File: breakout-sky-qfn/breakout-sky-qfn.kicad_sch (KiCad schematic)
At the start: 77 parts, among them J1 DF40C-50DS-0.4V_51, J2 DF40C-20DS-0.4V_51, J3 Conn_01x12, J4 Conn_01x12, J5 DF40C-40DS-0.4V_51, J7 DF40C-20DS-0.4V_51, U1 Openframe_QFN_TT06_REV2, U2 24LC02, U3 AP2112K-1.8, U4 AP2112K-1.8

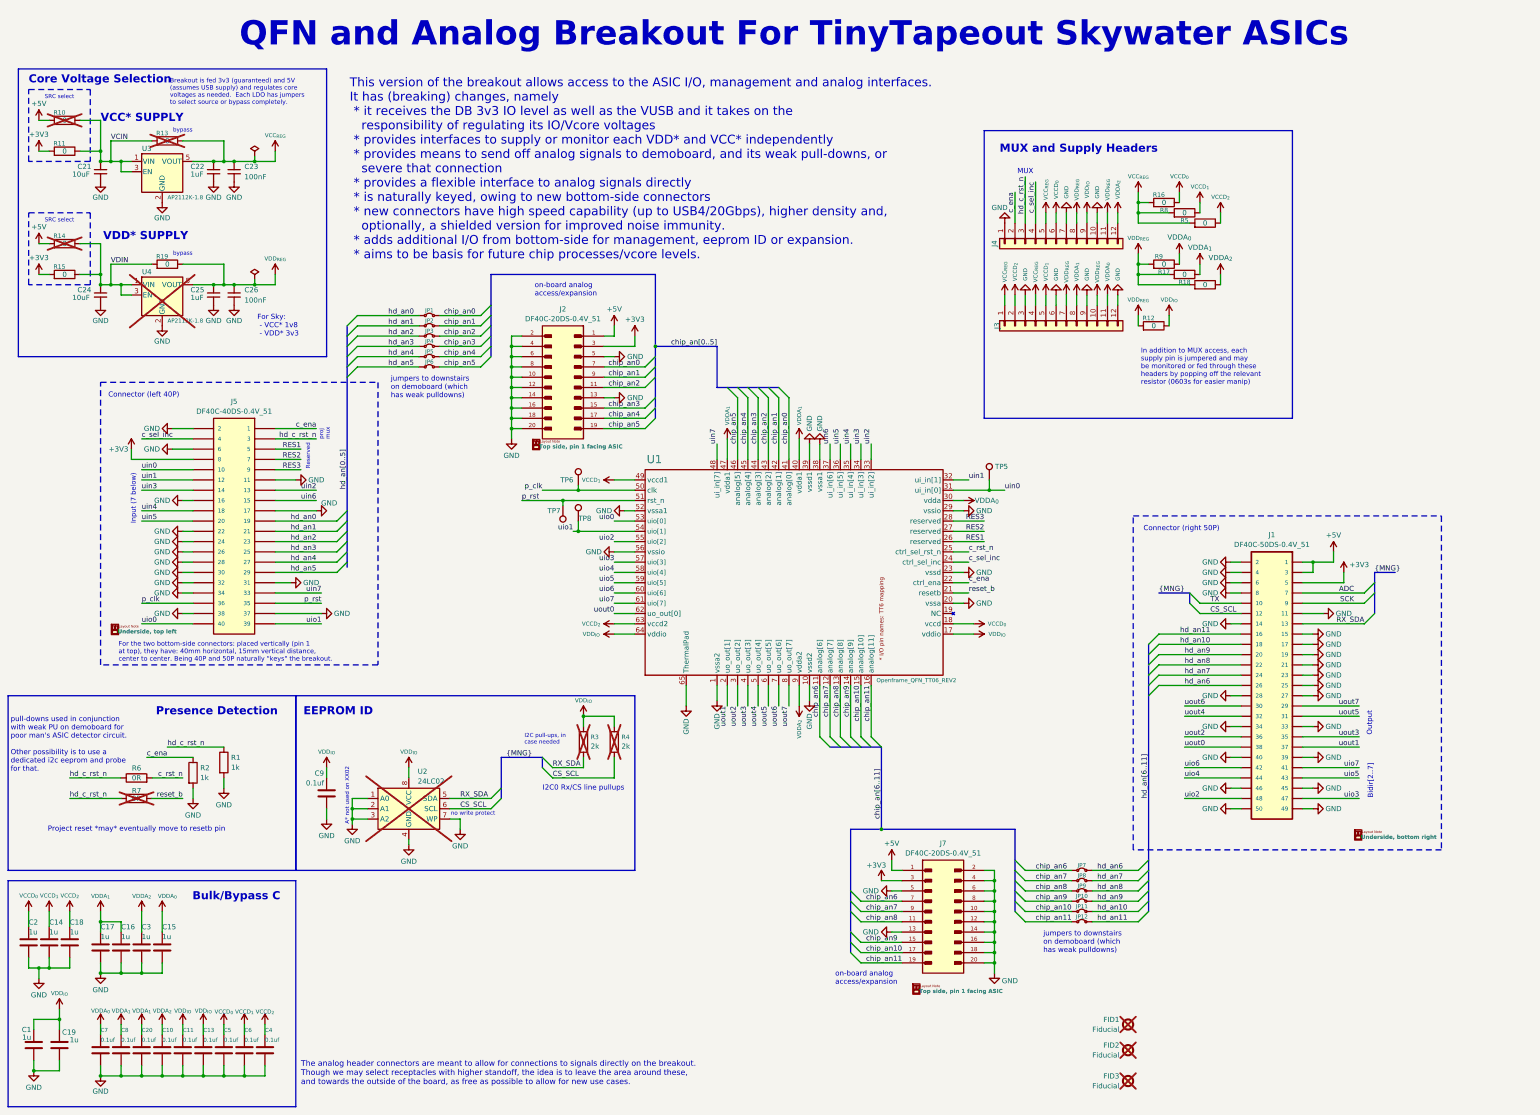
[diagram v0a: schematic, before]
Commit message: increased size of power rail jumpers
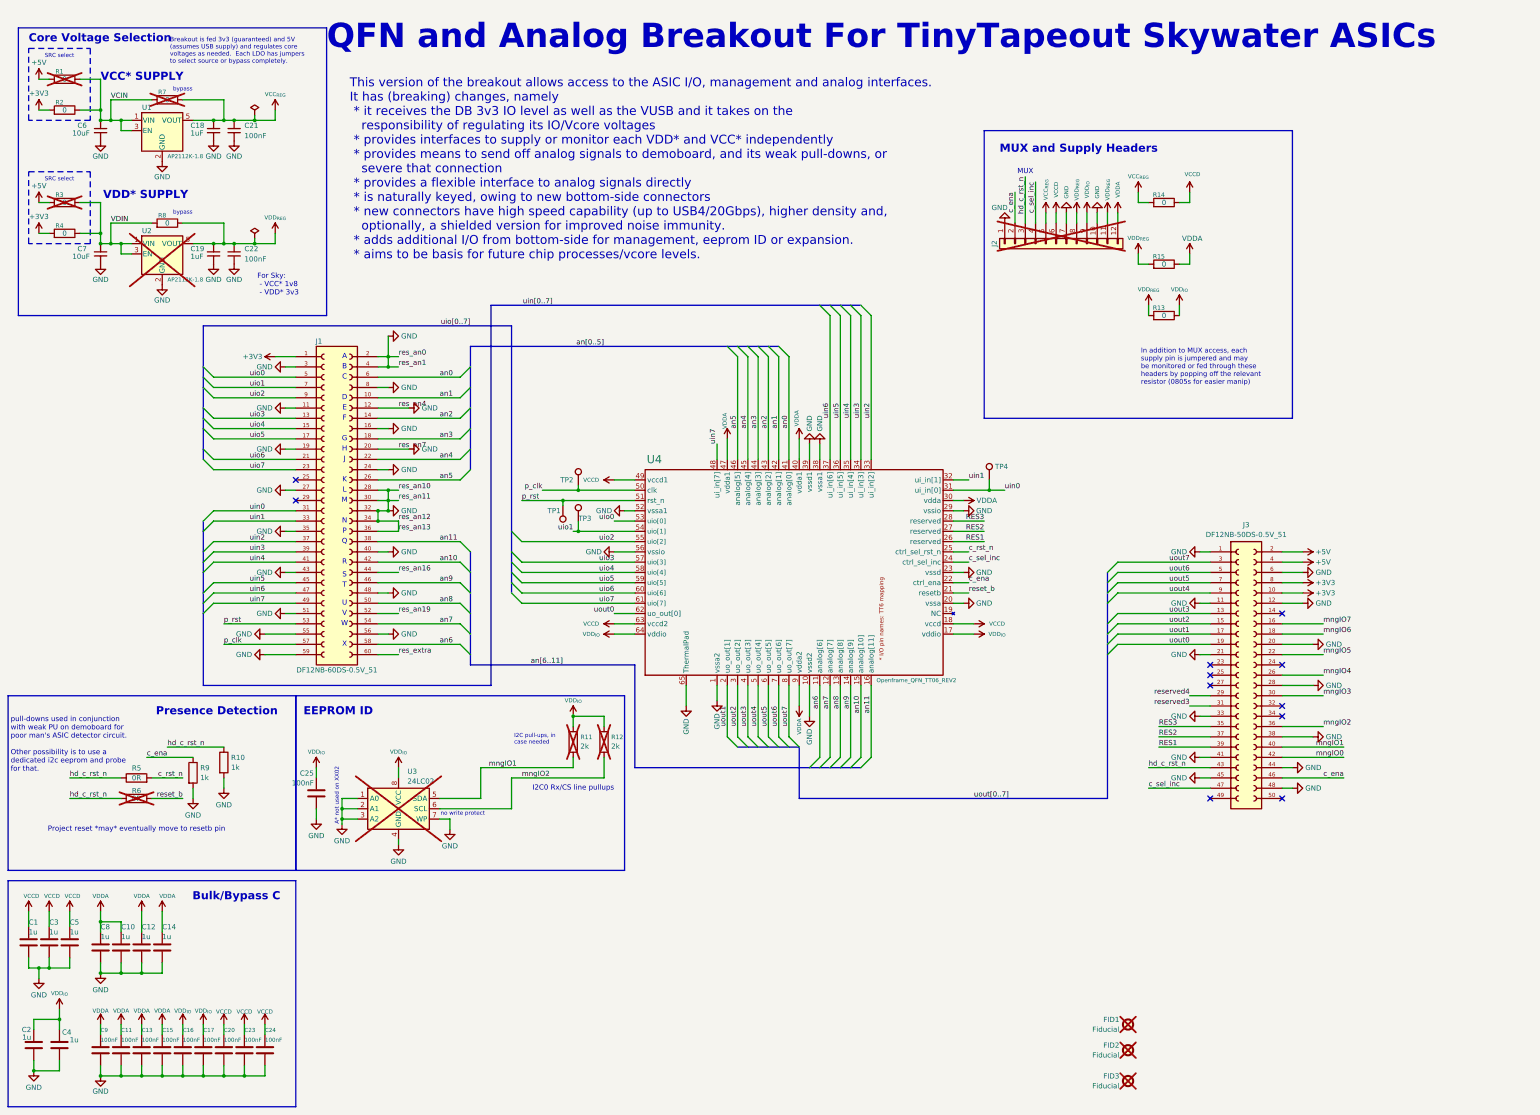
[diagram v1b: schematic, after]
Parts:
- removed J1: DF40C-50DS-0.4V_51, TinyTapeout:HRS_DF40C-50DS-0.4V_51, symbol TinyTapeout:DF40C-50DS-0.4V_51
- removed J2, J7: DF40C-20DS-0.4V_51, TinyTapeout:HRS_DF40C-20DP-0.4V_51, symbol TinyTapeout:DF40C-20DP-0.4V_51
- removed J3: Conn_01x12, Connector_PinHeader_2.54mm:PinHeader_1x12_P2.54mm_Vertical, symbol Connector_Generic:Conn_01x12
- removed J5: DF40C-40DS-0.4V_51, TinyTapeout:HIROSE_DF40C-40DS-0.4V_51, symbol TinyTapeout:DF40C-40DS-0.4V_51
- removed JP1, JP10, JP11, JP12, JP2, JP3, JP4, JP5, JP6, JP7, JP8, JP9: Jumper_2_Small_Bridged, TinyTapeout:SolderJumper-2_0603, symbol Jumper:Jumper_2_Small_Bridged
- removed LAYOUT1: Underside, top left, symbol psychogenic:LAYOUT
- removed LAYOUT2: Underside, bottom right, symbol psychogenic:LAYOUT
- removed LAYOUT3, LAYOUT4: Top side, pin 1 facing ASIC, symbol psychogenic:LAYOUT
- removed R17, R18, R5, R8: 0, Resistor_SMD:R_0603_1608Metric, symbol psycomponents:PsyResistors_IEC/R_0_0603_1608-46
- added J1: DF12NB-60DS-0.5V_51, TinyTapeout:HRS_DF12NB-60DS-0.5V_51, symbol TinyTapeout:DF12NB-60DS-0.5V_51
- added J3: DF12NB-50DS-0.5V_51, TinyTapeout:HRS_DF12NB-50DS-0.5V_51, symbol TinyTapeout:DF12NB-50DS-0.5V_51
- C1: renamed from C2; value C_1u_0603_50V -> 1uF; Characteristics 1u 0603 -> 1u 10V XR 0603
- C10: renamed from C16; value C_1u_0603_50V -> 1uF; Characteristics 1u 0603 -> 1u 10V XR 0603
- C11: renamed from C8; value 0.1uf -> 100nF; Characteristics 100n 0402 -> 100n 10% 25V XR 0402
- C12: renamed from C3; value C_1u_0603_50V -> 1uF; Characteristics 1u 0603 -> 1u 10V XR 0603
- C13: renamed from C20; value 0.1uf -> 100nF; Characteristics 100n 0402 -> 100n 10% 25V XR 0402
- C14: renamed from C15; value C_1u_0603_50V -> 1uF; Characteristics 1u 0603 -> 1u 10V XR 0603
- C15: renamed from C10; value 0.1uf -> 100nF; Characteristics 100n 0402 -> 100n 10% 25V XR 0402
- C16: renamed from C11; value 0.1uf -> 100nF; Characteristics 100n 0402 -> 100n 10% 25V XR 0402
- C17: renamed from C13; value 0.1uf -> 100nF; Characteristics 100n 0402 -> 100n 10% 25V XR 0402
- C2: renamed from C1; value C_1u_0603_50V -> 1uF; Characteristics 1u 0603 -> 1u 10V XR 0603
- C20: renamed from C5; value 0.1uf -> 100nF; Characteristics 100n 0402 -> 100n 10% 25V XR 0402
- C23: renamed from C6; value 0.1uf -> 100nF; Characteristics 100n 0402 -> 100n 10% 25V XR 0402
- C24: renamed from C4; value 0.1uf -> 100nF; Characteristics 100n 0402 -> 100n 10% 25V XR 0402
- C25: renamed from C9; value 0.1uf -> 100nF; Characteristics 100n 0402 -> 100n 10% 25V XR 0402
- C3: renamed from C14; value C_1u_0603_50V -> 1uF; Characteristics 1u 0603 -> 1u 10V XR 0603
- C4: renamed from C19; value C_1u_0603_50V -> 1uF; Characteristics 1u 0603 -> 1u 10V XR 0603
- C5: renamed from C18; value C_1u_0603_50V -> 1uF; Characteristics 1u 0603 -> 1u 10V XR 0603
- C8: renamed from C17; value C_1u_0603_50V -> 1uF; Characteristics 1u 0603 -> 1u 10V XR 0603
- C9: renamed from C7; value 0.1uf -> 100nF; Characteristics 100n 0402 -> 100n 10% 25V XR 0402
- J2: renamed from J4; now not fitted
- R10: renamed from R1; LCSC C202394 -> C11702; MPN (none) -> CR0402-FX-1001GLF
- R13: renamed from R12; footprint Resistor_SMD:R_0603_1608Metric -> Resistor_SMD:R_0805_2012Metric; Characteristics RES SMD 0 OHM JUMPER 1/10W 0603 -> RES SMD 0 OHM JUMPER 0805; DigikeyPN A106051CT-ND -> 13-RC0805JR-100RLCT-ND; LCSC (none) -> C4143065; MPN CRG0603ZR -> RC0805JR-100RL; Manufacturer TE Connectivity Passive Product -> (none); Package / Case 0603 (1608 Metric) -> (none)
- R14: renamed from R16; footprint Resistor_SMD:R_0603_1608Metric -> Resistor_SMD:R_0805_2012Metric; Characteristics RES SMD 0 OHM JUMPER 1/10W 0603 -> RES SMD 0 OHM JUMPER 0805; DigikeyPN A106051CT-ND -> 13-RC0805JR-100RLCT-ND; LCSC (none) -> C4143065; MPN CRG0603ZR -> RC0805JR-100RL; Manufacturer TE Connectivity Passive Product -> (none); Package / Case 0603 (1608 Metric) -> (none)
- R15: renamed from R9; footprint Resistor_SMD:R_0603_1608Metric -> Resistor_SMD:R_0805_2012Metric; Characteristics RES SMD 0 OHM JUMPER 1/10W 0603 -> RES SMD 0 OHM JUMPER 0805; DigikeyPN A106051CT-ND -> 13-RC0805JR-100RLCT-ND; LCSC (none) -> C4143065; MPN CRG0603ZR -> RC0805JR-100RL; Manufacturer TE Connectivity Passive Product -> (none); Package / Case 0603 (1608 Metric) -> (none)
- R2: renamed from R11; LCSC (none) -> C95177
- R4: renamed from R15; LCSC (none) -> C95177
- R8: renamed from R19; LCSC (none) -> C95177
- R9: renamed from R2; LCSC C202394 -> C11702; MPN (none) -> CR0402-FX-1001GLF
- U1: renamed from U3; Characteristics VREG 1.7V SOT-25 -> VREG 1.8V SOT-25
- U4: renamed from U1; LCSC (none) -> TT08_ASIC_CHIP
- renumbered C22 to C18, C25 to C19, C23 to C21, C26 to C22, C21 to C6, C24 to C7, R10 to R1, R3 to R11, R4 to R12, R14 to R3, R6 to R5, R7 to R6, R13 to R7, TP7 to TP1, TP6 to TP2, TP8 to TP3, TP5 to TP4, U4 to U2, U2 to U3
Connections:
- net VCCD_{1} is gone; now on net VCCD: C23.1, C3.1, U4.49 (vccd1)
- net VCCD_{2} is gone; now on net VCCD: C24.2, C5.1, U4.63 (vccd2)
- net VDDA_{1} is gone; now on net VDDA: C10.1, C11.2, C13.2, C8.1, U4.40 (vdda1), U4.47 (vdda1)
- net VDDA_{2} is gone; now on net VDDA: C12.1, C15.1, J2.12 (Pin_12), U4.9 (vdda2)
- net +3V3: now also J1.1, J3.10, J3.8
- net +5V: now also J3.2, J3.4
- net GND: now also J1.11, J1.12, J1.16, J1.19, J1.2, J1.20, J1.24, J1.27, J1.28, J1.3, J1.30, J1.32, J1.34, J1.35, J1.36, J1.4, J1.40, J1.43, J1.48, J1.51, J1.55, J1.56, J1.59, J1.8, J3.1, J3.11, J3.12, J3.20, J3.21, J3.28, J3.33, J3.38, J3.41, J3.44, J3.45, J3.48, J3.6
- net RES1: now also J3.39
- net RES2: now also J3.37
- net RES3: now also J3.35
- net c_ena: now also J3.46
- net c_sel_inc: now also J3.47
- net hd_c_rst_n: now also J3.43
- net p_clk: now also J1.57
- net p_rst: now also J1.53
- net uin0: now also J1.31
- net uin1: now also J1.33
- net uin2: now also J1.37
- net uin3: now also J1.39
- net uin4: now also J1.41
- net uin5: now also J1.45
- net uin6: now also J1.47
- net uin7: now also J1.49
- net uio0: now also J1.5
- net uio1: now also J1.7
- net uio2: now also J1.9
- net uio3: now also J1.13
- net uio4: now also J1.15
- net uio5: now also J1.17
- net uio6: now also J1.21
- net uio7: now also J1.23
- net uout0: now also J3.19
- net uout1: now also J3.17
- net uout2: now also J3.15
- net uout3: now also J3.13
- net uout4: now also J3.9
- net uout5: now also J3.7
- net uout6: now also J3.5
- net uout7: now also J3.3
- net CS_SCL renamed mngIO2
- net mngIO2: now also J3.36
- net RX_SDA renamed mngIO1
- net mngIO1: now also J3.40
- net VCCD_{0} renamed VCCD
- net VDDA_{0} renamed VDDA
- net chip_an0 renamed an0
- net an0: now also J1.6
- net chip_an1 renamed an1
- net an1: now also J1.10
- net chip_an10 renamed an10
- net an10: now also J1.42
- net chip_an11 renamed an11
- net an11: now also J1.38
- net chip_an2 renamed an2
- net an2: now also J1.14
- net chip_an3 renamed an3
- net an3: now also J1.18
- net chip_an4 renamed an4
- net an4: now also J1.22
- net chip_an5 renamed an5
- net an5: now also J1.26
- net chip_an6 renamed an6
- net an6: now also J1.58
- net chip_an7 renamed an7
- net an7: now also J1.54
- net chip_an8 renamed an8
- net an8: now also J1.50
- net chip_an9 renamed an9
- net an9: now also J1.46
- new net mngIO0: J3.42
- new net mngIO3: J3.30
- new net mngIO4: J3.26
- new net mngIO5: J3.22
- new net mngIO6: J3.18
- new net mngIO7: J3.16
- new net res_an16: J1.44
- new net res_an19: J1.52
- new net res_extra: J1.60
- new net reserved3: J3.31
- new net reserved4: J3.29
- no-connect marks 0 -> 11
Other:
- note added: "A"
- note added: "B"
- note added: "C"
- note added: "D"
- note added: "E"
- note added: "F"
- note added: "G"
- note added: "H"
- note added: "In addition to MUX access, each supply pin is jumpered and may be monitored or fed through these headers by popping off the relevant resistor (0805s for easier manip)"
- note added: "J"
- note added: "K"
- note added: "L"
- note added: "M"
- note added: "N"
- note added: "P"
- note added: "Q"
- note added: "R"
- note added: "S"
- note added: "T"
- note added: "U"
- note added: "V"
- note added: "W"
- note added: "X"
- note removed: "Bidir[2..7]"
- note removed: "Connector (left 40P)"
- note removed: "Connector (right 50P)"
- note removed: "For the two bottom-side connectors: placed vertically (pin 1 at top), they have: 40mm horizontal, 15mm vertical distance, center to center. Being 40P and 50P naturally "keys" the breakout."
- note removed: "In addition to MUX access, each supply pin is jumpered and may be monitored or fed through these headers by popping off the relevant resistor (0603s for easier manip)"
- note removed: "Input (7 below)"
- note removed: "Output"
- note removed: "Reserved"
- note removed: "The analog header connectors are meant to allow for connections to signals directly on the breakout. Though we may select receptacles with higher standoff, the idea is to leave the area around these, and towards the outside of the board, as free as possible to allow for new use cases."
- note removed: "jumpers to downstairs on demoboard (which has weak pulldowns)"
- note removed: "on-board analog access/expansion"
- note removed: "proj mux"
- moved on the sheet: C18, C19, C21, C22, C25, C6, C7, R1, R11, R12, R13, R2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

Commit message: sky breakout layout tweaks, v3.2
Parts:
- C18, C19: MPN CL10A105KA8NNNC -> GRT188R61H105KE13D
- U4: LCSC TT08_ASIC_CHIP -> TT_ASIC_CHIP
